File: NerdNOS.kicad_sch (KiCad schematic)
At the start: 3 parts, among them J3 USB_C_Receptacle_USB2.0

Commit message: routing wok
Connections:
- net GND: no longer J3.B4 (VBUS)
- net Power/VIN renamed 5V
- net 5V: now also J3.B4 (VBUS)
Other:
- sheet BM1397 ports: added CLKI; removed none
- sheet Power ports: added 1V4, 3V3, 5V; removed VIN, VOUT
- sheet T_Display_S3 ports: added BI, CLKI; removed none
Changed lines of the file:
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@@
 	(paper "A4")
+	(junction
+		(at 172.72 74.93)
+		(diameter 0)
+		(color 0 0 0 0)
+	)
 	(junction
 		(at 238.76 119.38)
@@
 		(color 0 0 0 0)
 	)
+	(junction
+		(at 237.49 99.06)
+		(diameter 0)
+		(color 0 0 0 0)
+	)
 	(no_connect
 		(at 213.36 125.73)
@@
 	(wire
 		(pts
+			(xy 172.72 74.93) (xy 172.72 63.5)
+		)
+		(stroke
+			(width 0)
+			(type default)
+		)
+	)
+	(wire
+		(pts
 			(xy 232.41 106.68) (xy 245.11 106.68)
 		)
@@
 	(wire
 		(pts
+			(xy 76.2 128.27) (xy 99.06 128.27)
+		)
+		(stroke
+			(width 0)
+			(type default)
+		)
+	)
+	(wire
+		(pts
+			(xy 152.4 76.2) (xy 85.09 76.2)
+		)
+		(stroke
+			(width 0)
+			(type default)
+		)
+	)
+	(wire
+		(pts
 			(xy 238.76 119.38) (xy 245.11 119.38)
 		)
@@
 	(wire
 		(pts
-			(xy 234.95 100.33) (xy 237.49 100.33)
-		)
-		(stroke
-			(width 0)
-			(type default)
-		)
-	)
-	(wire
-		(pts
 			(xy 213.36 125.73) (xy 236.22 125.73)
 		)
@@
 	(wire
 		(pts
-			(xy 237.49 100.33) (xy 237.49 101.6)
+			(xy 76.2 63.5) (xy 76.2 128.27)
+		)
+		(stroke
+			(width 0)
+			(type default)
+		)
+	)
+	(wire
+		(pts
+			(xy 172.72 74.93) (xy 167.64 74.93)
+		)
+		(stroke
+			(width 0)
+			(type default)
+		)
+	)
+	(wire
+		(pts
+			(xy 237.49 99.06) (xy 237.49 101.6)
+		)
+		(stroke
+			(width 0)
+			(type default)
+		)
+	)
+	(wire
+		(pts
+			(xy 125.73 125.73) (xy 156.21 125.73)
 		)
 		(stroke
@@
 	(wire
 		(pts
+			(xy 85.09 121.92) (xy 99.06 121.92)
+		)
+		(stroke
+			(width 0)
+			(type default)
+		)
+	)
+	(wire
+		(pts
+			(xy 172.72 63.5) (xy 76.2 63.5)
+		)
+		(stroke
+			(width 0)
+			(type default)
+		)
+	)
+	(wire
+		(pts
 			(xy 220.98 104.14) (xy 245.11 104.14)
 		)
@@
 	(wire
 		(pts
+			(xy 85.09 76.2) (xy 85.09 121.92)
+		)
+		(stroke
+			(width 0)
+			(type default)
+		)
+	)
+	(wire
+		(pts
 			(xy 245.11 111.76) (xy 236.22 111.76)
 		)
@@
 	(wire
 		(pts
-			(xy 186.69 80.01) (xy 167.64 80.01)
+			(xy 186.69 74.93) (xy 172.72 74.93)
+		)
+		(stroke
+			(width 0)
+			(type default)
+		)
+	)
+	(wire
+		(pts
+			(xy 125.73 129.54) (xy 156.21 129.54)
 		)
 		(stroke
@@
 	(wire
 		(pts
-			(xy 186.69 80.01) (xy 186.69 99.06)
-		)
-		(stroke
-			(width 0)
-			(type default)
-		)
-	)
-	(wire
-		(pts
-			(xy 186.69 99.06) (xy 245.11 99.06)
+			(xy 186.69 74.93) (xy 186.69 99.06)
+		)
+		(stroke
+			(width 0)
+			(type default)
+		)
+	)
+	(wire
+		(pts
+			(xy 186.69 99.06) (xy 237.49 99.06)
 		)
 		(stroke
@@
 			(width 0)
 			(type default)
+		)
+	)
+	(wire
+		(pts
+			(xy 237.49 99.06) (xy 245.11 99.06)
+		)
+		(stroke
+			(width 0)
+			(type default)
+		)
+	)
+	(label "5V"
+		(at 196.85 99.06 0)
+		(fields_autoplaced yes)
+		(effects
+			(font
+				(size 1.27 1.27)
+			)
+			(justify left bottom)
 		)
 	)
@@
 	)
 	(symbol
-		(lib_id "power:GND")
-		(at 234.95 100.33 0)
-		(unit 1)
-		(exclude_from_sim no)
-		(in_bom yes)
-		(on_board yes)
-		(dnp no)
-		(fields_autoplaced yes)
-		(property "Reference" "#PWR05"
-			(at 234.95 106.68 0)
-			(effects
-				(font
-					(size 1.27 1.27)
-				)
-				(hide yes)
-			)
-		)
-		(property "Value" "GND"
-			(at 234.95 105.41 0)
-			(effects
-				(font
-					(size 1.27 1.27)
-				)
-			)
-		)
-		(property "Footprint" ""
-			(at 234.95 100.33 0)
-			(effects
-				(font
-					(size 1.27 1.27)
-				)
-				(hide yes)
-			)
-		)
-		(property "Datasheet" ""
-			(at 234.95 100.33 0)
-			(effects
-				(font
-					(size 1.27 1.27)
-				)
-				(hide yes)
-			)
-		)
-		(property "Description" "Power symbol creates a global label with name \"GND\" , ground"
-			(at 234.95 100.33 0)
-			(effects
-				(font
-					(size 1.27 1.27)
-				)
-				(hide yes)
-			)
-		)
-		(pin "1"
-		)
-		(instances
-			(project "NerdNOS"
-				(path "/d95c6d04-3717-413a-8b9f-685b8757ddd5"
-					(reference "#PWR05")
-					(unit 1)
-				)
-			)
-		)
-	)
-	(symbol
 		(lib_id "Device:R_US")
 		(at 228.6 106.68 90)
@@
 			)
 		)
-		(pin "5V" input
-			(at 99.06 124.46 180)
-			(effects
-				(font
-					(size 1.27 1.27)
-				)
-				(justify left)
-			)
-		)
 		(pin "TX" input
 			(at 125.73 118.11 0)
@@
 		)
 		(pin "BI" input
-			(at 99.06 113.03 180)
-			(effects
-				(font
-					(size 1.27 1.27)
-				)
-				(justify left)
+			(at 125.73 125.73 0)
+			(effects
+				(font
+					(size 1.27 1.27)
+				)
+				(justify right)
 			)
 		)
@@
 				)
 				(justify right)
+			)
+		)
+		(pin "CLKI" input
+			(at 125.73 129.54 0)
+			(effects
+				(font
+					(size 1.27 1.27)
+				)
+				(justify right)
+			)
+		)
+		(pin "5V" input
+			(at 99.06 128.27 180)
+			(effects
+				(font
+					(size 1.27 1.27)
+				)
+				(justify left)
 			)
 		)
@@
 			)
 		)
-		(pin "VOUT" input
+		(pin "5V" input
+			(at 167.64 74.93 0)
+			(effects
+				(font
+					(size 1.27 1.27)
+				)
+				(justify right)
+			)
+		)
+		(pin "3V3" output
+			(at 152.4 76.2 180)
+			(effects
+				(font
+					(size 1.27 1.27)
+				)
+				(justify left)
+			)
+		)
+		(pin "1V4" input
 			(at 152.4 78.74 180)
 			(effects
@@
 				)
 				(justify left)
-			)
-		)
-		(pin "VIN" input
-			(at 167.64 80.01 0)
-			(effects
-				(font
-					(size 1.27 1.27)
-				)
-				(justify right)
 			)
 		)
@@
 			(effects
 				(font
+					(size 1.27 1.27)
+				)
+				(justify left)
+			)
+		)
+		(pin "BI" input
+			(at 156.21 125.73 180)
+			(effects
+				(font
+					(size 1.27 1.27)
+				)
+				(justify left)
+			)
+		)
+		(pin "CLKI" input
+			(at 156.21 129.54 180)
+			(effects
+				(font

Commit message: routing work
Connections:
- net 5V renamed BM1397/VBUS
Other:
- sheet BM1397 ports: added VBUS; removed 5V
- sheet Power ports: added VBUS; removed 5V
- sheet T_Display_S3 ports: added VBUS; removed 5V
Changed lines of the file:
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@@
-		)
-	)
-	(label "5V"
-		(at 196.85 99.06 0)
-		(fields_autoplaced yes)
-		(effects
-			(font
-				(size 1.27 1.27)
-			)
-			(justify left bottom)
 		)
 	)
@@
 			)
 		)
-		(pin "5V" input
+		(pin "VBUS" input
 			(at 99.06 128.27 180)
 			(effects
@@
 			)
 		)
-		(pin "5V" input
+		(pin "VBUS" input
 			(at 167.64 74.93 0)
 			(effects
@@
 			)
 		)
-		(pin "5V" input
+		(pin "VBUS" input
 			(at 181.61 120.65 0)
 			(effects

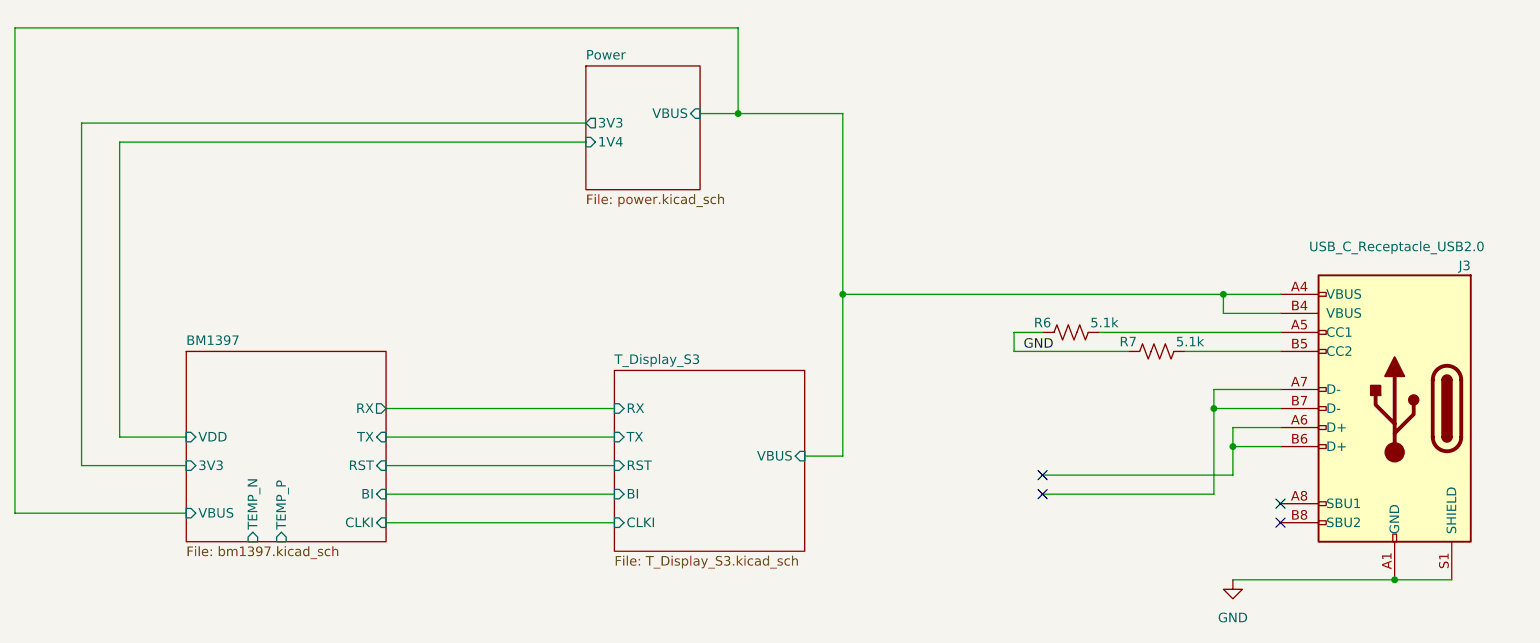
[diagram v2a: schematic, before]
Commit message: replace inductor, tant cap, remove 3v3
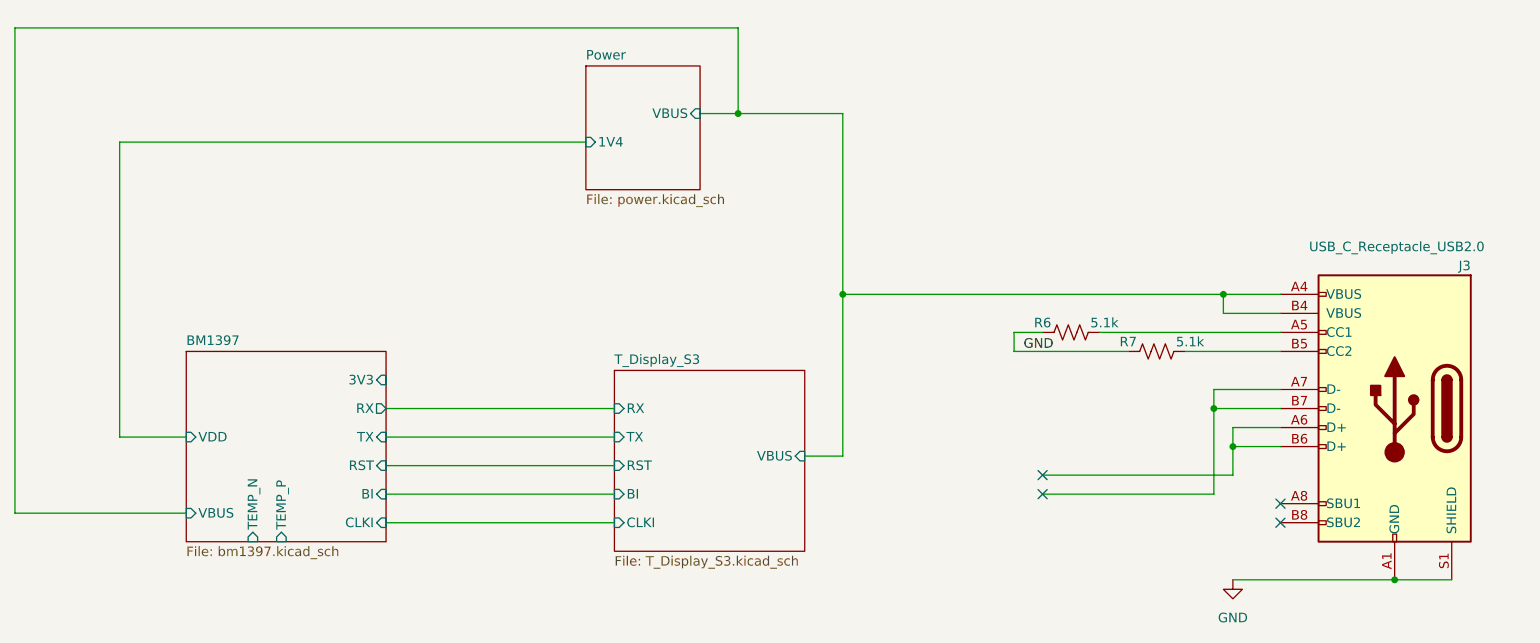
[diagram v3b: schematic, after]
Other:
- sheet Power ports: added none; removed 3V3
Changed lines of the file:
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@@
-	(wire
-		(pts
-			(xy 152.4 76.2) (xy 85.09 76.2)
-		)
-		(stroke
-			(width 0)
-			(type default)
-		)
-	)
 	(wire
 		(pts
@@
 	(wire
 		(pts
-			(xy 85.09 121.92) (xy 99.06 121.92)
-		)
-		(stroke
-			(width 0)
-			(type default)
-		)
-	)
-	(wire
-		(pts
 			(xy 172.72 63.5) (xy 76.2 63.5)
 		)
@@
 		(pts
 			(xy 220.98 104.14) (xy 245.11 104.14)
-		)
-		(stroke
-			(width 0)
-			(type default)
-		)
-	)
-	(wire
-		(pts
-			(xy 85.09 76.2) (xy 85.09 121.92)
 		)
 		(stroke
@@
 		)
 		(pin "3V3" input
-			(at 99.06 121.92 180)
-			(effects
-				(font
-					(size 1.27 1.27)
-				)
-				(justify left)
+			(at 125.73 110.49 0)
+			(effects
+				(font
+					(size 1.27 1.27)
+				)
+				(justify right)
 			)
 		)
@@
 			)
 		)
-		(pin "3V3" output
-			(at 152.4 76.2 180)
-			(effects
-				(font
-					(size 1.27 1.27)
-				)
-				(justify left)
-			)
-		)

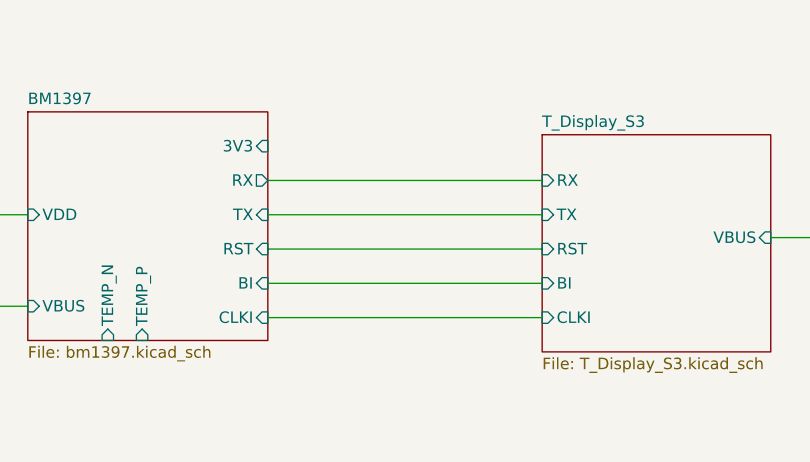
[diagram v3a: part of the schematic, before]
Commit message: BI pulldown
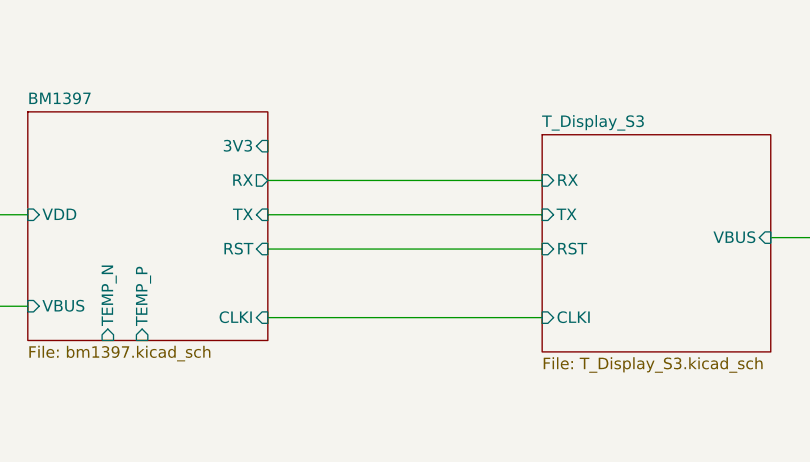
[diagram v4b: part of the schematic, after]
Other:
- sheet BM1397 ports: added none; removed BI
- sheet T_Display_S3 ports: added none; removed BI
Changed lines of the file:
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@@
-	(wire
-		(pts
-			(xy 125.73 125.73) (xy 156.21 125.73)
-		)
-		(stroke
-			(width 0)
-			(type default)
-		)
-	)
 	(wire
 		(pts
@@
 			)
 		)
-		(pin "BI" input
-			(at 125.73 125.73 0)
-			(effects
-				(font
-					(size 1.27 1.27)
-				)
-				(justify right)
-			)
-		)
 		(pin "RX" output
 			(at 125.73 114.3 0)
@@
 			(effects
 				(font
-					(size 1.27 1.27)
-				)
-				(justify left)
-			)
-		)
-		(pin "BI" input
-			(at 156.21 125.73 180)
-			(effects
-				(font

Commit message: level shifter
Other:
- sheet T_Display_S3 ports: added 3V3; removed none
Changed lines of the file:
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@@
+	(wire
+		(pts
+			(xy 152.4 115.57) (xy 152.4 118.11)
+		)
+		(stroke
+			(width 0)
+			(type default)
+		)
+	)
 	(wire
 		(pts
@@
 	(wire
 		(pts
-			(xy 181.61 120.65) (xy 186.69 120.65)
+			(xy 181.61 118.11) (xy 186.69 118.11)
 		)
 		(stroke
@@
 	(wire
 		(pts
+			(xy 156.21 109.22) (xy 125.73 109.22)
+		)
+		(stroke
+			(width 0)
+			(type default)
+		)
+	)
+	(wire
+		(pts
 			(xy 236.22 111.76) (xy 236.22 114.3)
 		)
@@
 	(wire
 		(pts
+			(xy 153.67 121.92) (xy 125.73 121.92)
+		)
+		(stroke
+			(width 0)
+			(type default)
+		)
+	)
+	(wire
+		(pts
 			(xy 224.79 106.68) (xy 209.55 106.68)
 		)
@@
 	(wire
 		(pts
-			(xy 125.73 118.11) (xy 156.21 118.11)
+			(xy 152.4 115.57) (xy 156.21 115.57)
 		)
 		(stroke
@@
 	(wire
 		(pts
+			(xy 154.94 127) (xy 154.94 129.54)
+		)
+		(stroke
+			(width 0)
+			(type default)
+		)
+	)
+	(wire
+		(pts
 			(xy 76.2 63.5) (xy 76.2 128.27)
 		)
@@
 	(wire
 		(pts
+			(xy 151.13 111.76) (xy 151.13 114.3)
+		)
+		(stroke
+			(width 0)
+			(type default)
+		)
+	)
+	(wire
+		(pts
 			(xy 172.72 74.93) (xy 167.64 74.93)
 		)
@@
 	(wire
 		(pts
+			(xy 151.13 114.3) (xy 125.73 114.3)
+		)
+		(stroke
+			(width 0)
+			(type default)
+		)
+	)
+	(wire
+		(pts
+			(xy 152.4 118.11) (xy 125.73 118.11)
+		)
+		(stroke
+			(width 0)
+			(type default)
+		)
+	)
+	(wire
+		(pts
 			(xy 237.49 99.06) (xy 237.49 101.6)
 		)
@@
 	(wire
 		(pts
+			(xy 153.67 119.38) (xy 153.67 121.92)
+		)
+		(stroke
+			(width 0)
+			(type default)
+		)
+	)
+	(wire
+		(pts
 			(xy 172.72 63.5) (xy 76.2 63.5)
 		)
@@
 	(wire
 		(pts
+			(xy 154.94 129.54) (xy 125.73 129.54)
+		)
+		(stroke
+			(width 0)
+			(type default)
+		)
+	)
+	(wire
+		(pts
 			(xy 245.11 111.76) (xy 236.22 111.76)
 		)
@@
 	(wire
 		(pts
-			(xy 125.73 121.92) (xy 156.21 121.92)
-		)
-		(stroke
-			(width 0)
-			(type default)
-		)
-	)
-	(wire
-		(pts
-			(xy 125.73 114.3) (xy 156.21 114.3)
+			(xy 153.67 119.38) (xy 156.21 119.38)
+		)
+		(stroke
+			(width 0)
+			(type default)
+		)
+	)
+	(wire
+		(pts
+			(xy 151.13 111.76) (xy 156.21 111.76)
 		)
 		(stroke
@@
 	(wire
 		(pts
-			(xy 186.69 99.06) (xy 186.69 120.65)
+			(xy 186.69 99.06) (xy 186.69 118.11)
 		)
 		(stroke
@@
 	(wire
 		(pts
-			(xy 125.73 129.54) (xy 156.21 129.54)
+			(xy 154.94 127) (xy 156.21 127)
 		)
 		(stroke
@@
 		)
 		(pin "3V3" input
-			(at 125.73 110.49 0)
+			(at 125.73 109.22 0)
 			(effects
 				(font
@@
 	)
 	(sheet
-		(at 156.21 109.22)
+		(at 156.21 106.68)
 		(size 25.4 24.13)
 		(fields_autoplaced yes)
@@
 		)
 		(property "Sheetname" "T_Display_S3"
-			(at 156.21 108.5084 0)
+			(at 156.21 105.9684 0)
 			(effects
 				(font
@@
 		)
 		(property "Sheetfile" "T_Display_S3.kicad_sch"
-			(at 156.21 133.9346 0)
+			(at 156.21 131.3946 0)
 			(effects
 				(font
@@
 		)
 		(pin "VBUS" input
-			(at 181.61 120.65 0)
+			(at 181.61 118.11 0)
 			(effects
 				(font
@@
 		)
 		(pin "RX" input
-			(at 156.21 114.3 180)
+			(at 156.21 111.76 180)
 			(effects
 				(font
@@
 		)
 		(pin "TX" input
-			(at 156.21 118.11 180)
+			(at 156.21 115.57 180)
 			(effects
 				(font
@@
 		)
 		(pin "RST" input
-			(at 156.21 121.92 180)
+			(at 156.21 119.38 180)
 			(effects
 				(font
@@
 		)
 		(pin "CLKI" input
-			(at 156.21 129.54 180)
-			(effects
-				(font
+			(at 156.21 127 180)
+			(effects
+				(font
+					(size 1.27 1.27)
+				)
+				(justify left)
+			)
+		)
+		(pin "3V3" input
+			(at 156.21 109.22 180)
+			(effects
+				(font

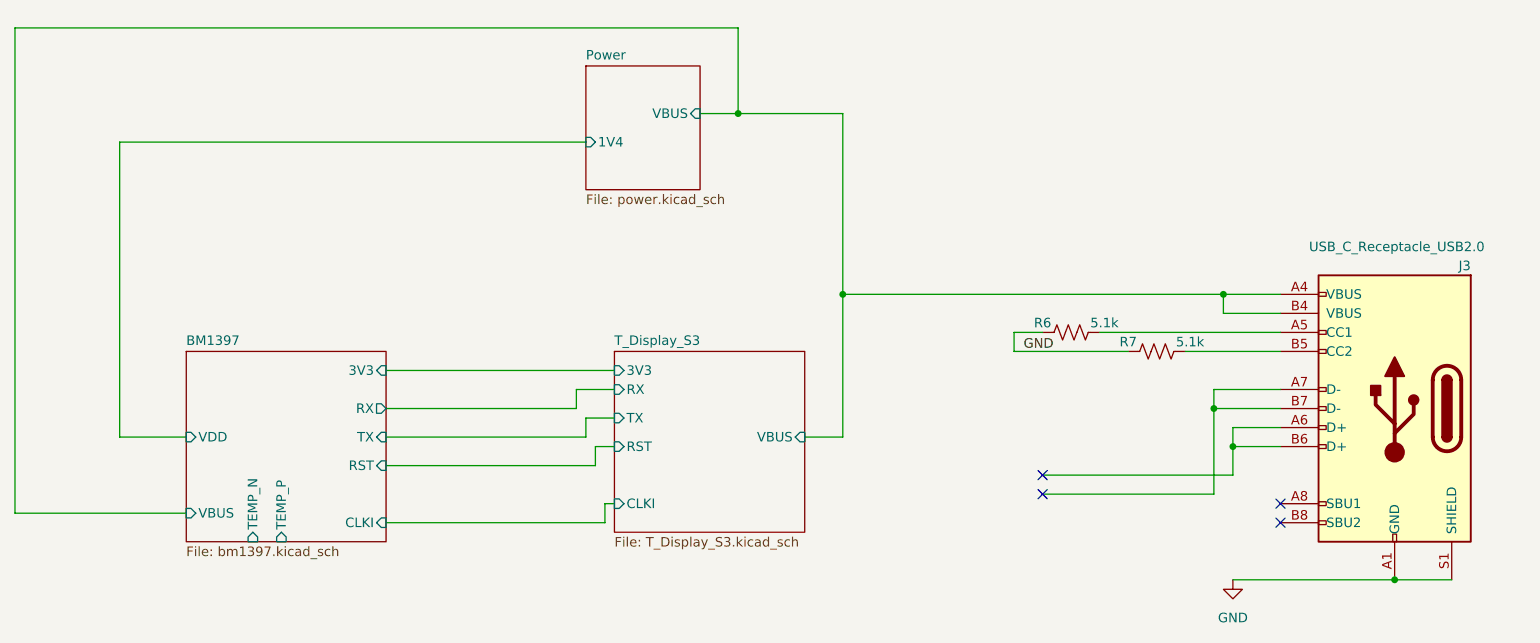
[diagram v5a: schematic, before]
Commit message: schematic and symbol cleanup. detached CLKI from ESP32.
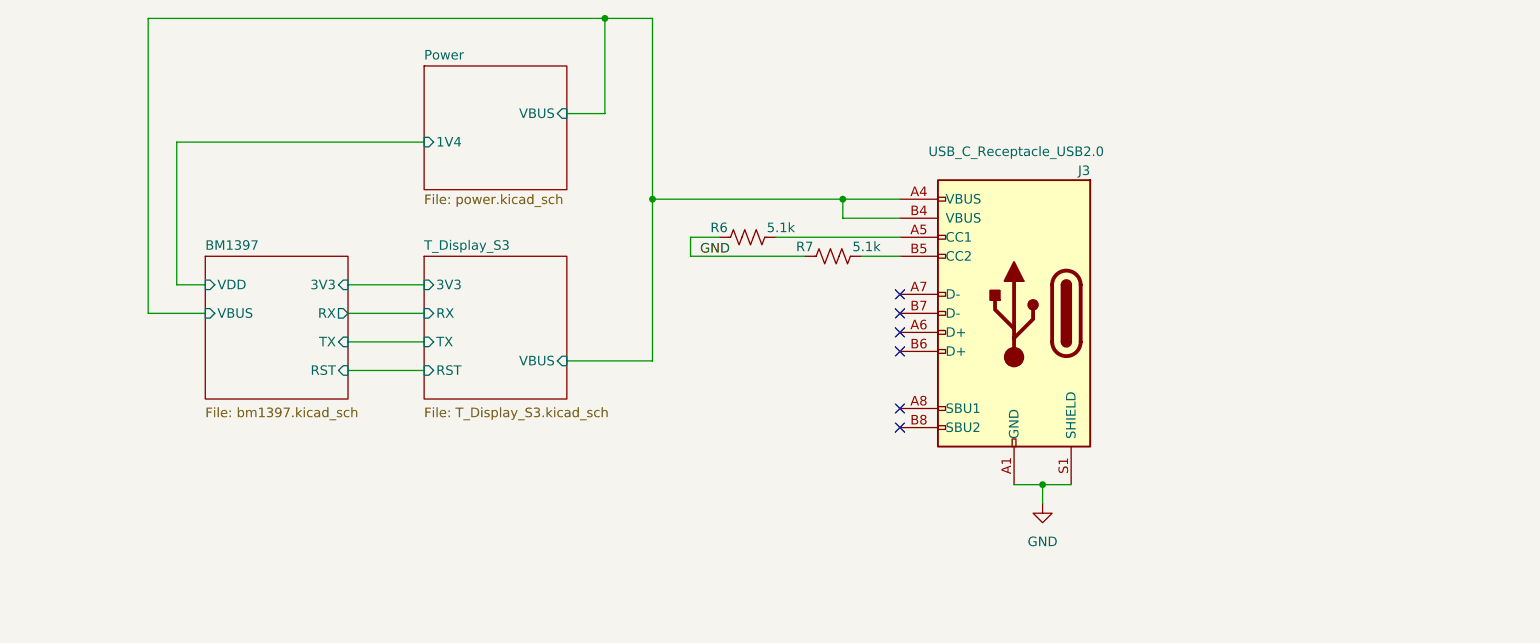
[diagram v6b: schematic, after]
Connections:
- net at J3.A6 (D+): no longer J3.B6 (D+)
- net at J3.A7 (D-): no longer J3.B7 (D-)
- no-connect marks 4 -> 6
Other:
- sheet BM1397 ports: added none; removed CLKI, TEMP_N, TEMP_P
- sheet T_Display_S3 ports: added none; removed CLKI
- title: (none) -> NerdNOS
- moved on the sheet: J3, R6, R7

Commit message: added 3d shapes. pcb cleanup
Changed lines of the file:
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@@
 			)
 		)
-		(property "Description" ""
+		(property "Description" "USB 2.0-only Type-C Receptacle connector"
 			(at 209.55 101.6 0)
 			(effects
@@
 			)
 		)
-		(pin "1V4" input
+		(pin "1V4" output
 			(at 130.81 78.74 180)
 			(effects
@@
 			)
 		)
-		(pin "TX" input
+		(pin "TX" output
 			(at 130.81 105.41 180)
 			(effects
@@
 			)
 		)
-		(pin "RST" input
+		(pin "RST" output
 			(at 130.81 109.22 180)
 			(effects
@@
 			)
 		)
-		(pin "3V3" input
+		(pin "3V3" output
 			(at 130.81 97.79 180)
 			(effects

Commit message: thermistor
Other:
- sheet BM1397 ports: added TMP; removed none
- sheet T_Display_S3 ports: added TMP; removed none
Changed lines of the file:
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@@
+	(wire
+		(pts
+			(xy 120.65 113.03) (xy 130.81 113.03)
+		)
+		(stroke
+			(width 0)
+			(type default)
+		)
+	)
 	(wire
 		(pts
@@
 	(sheet
 		(at 101.6 93.98)
-		(size 19.05 19.05)
+		(size 19.05 22.86)
 		(fields_autoplaced yes)
 		(stroke
@@
 		)
 		(property "Sheetfile" "bm1397.kicad_sch"
-			(at 101.6 114.1226 0)
+			(at 101.6 117.4246 0)
 			(effects
 				(font
@@
 				)
 				(justify left)
+			)
+		)
+		(pin "TMP" output
+			(at 120.65 113.03 0)
+			(effects
+				(font
+					(size 1.27 1.27)
+				)
+				(justify right)
 			)
 		)
@@
 	(sheet
 		(at 130.81 93.98)
-		(size 19.05 19.05)
+		(size 19.05 22.86)
 		(fields_autoplaced yes)
 		(stroke
@@
 		)
 		(property "Sheetfile" "T_Display_S3.kicad_sch"
-			(at 130.81 114.1226 0)
+			(at 130.81 117.4246 0)
 			(effects
 				(font
@@
 			(effects
 				(font
+					(size 1.27 1.27)
+				)
+				(justify left)
+			)
+		)
+		(pin "TMP" input
+			(at 130.81 113.03 180)
+			(effects
+				(font
